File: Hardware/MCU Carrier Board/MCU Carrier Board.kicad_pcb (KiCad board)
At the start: 2 copper layers, 31.8 x 50.8 mm, 27 parts, among them J1 Conn_01x06_Pin, J2 Conn_01x06_Pin, J3 Conn_01x06_Pin, J4 Top Connector, J5 Bottom Connector, J6 Conn_01x06_Pin, J7 Conn_01x06_Pin, J8 Conn_01x06_Pin, SW3 SW_Push, SW4 SW_Push, SW5 SW_Push

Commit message: update
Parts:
- C1, C2, C3, C4: footprint Capacitor_SMD:C_0603_1608Metric_Pad1.08x0.95mm_HandSolder -> MCU Carrier board:C_0603_1608Metric_Pad1.08x0.95mm_HandSolder
- D1, D2, D3, D4: footprint LED_SMD:LED_0603_1608Metric_Pad1.05x0.95mm_HandSolder -> MCU Carrier board:LED_0603_1608Metric_Pad1.05x0.95mm_HandSolder
- H1, H2, H3, H4: footprint MountingHole:MountingHole_2.5mm -> MCU Carrier board:MountingHole_2.5mm
- J1, J2, J3, J6, J7, J8: footprint Connector_PinHeader_1.27mm:PinHeader_1x06_P1.27mm_Vertical -> MCU Carrier board:PinHeader_1x06_P1.27mm_Vertical
- J4, J5: footprint DF40C:HRS_DF40C-20DS-0.4V_51_ -> MCU Carrier board:HRS_DF40C-20DS-0.4V_51_
- R1, R2, R3, R4: footprint Resistor_SMD:R_0603_1608Metric_Pad0.98x0.95mm_HandSolder -> MCU Carrier board:R_0603_1608Metric_Pad0.98x0.95mm_HandSolder
- SW3, SW4, SW5: footprint Button_Switch_SMD:SW_Push_1P1T_XKB_TS-1187A -> MCU Carrier board:SW_Push_1P1T_XKB_TS-1187A
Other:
- board text added: "MCU R V1 10/25"
- board text added: "Up"

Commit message: update
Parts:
- C1, C2, C3, C4: footprint MCU Carrier board:C_0603_1608Metric_Pad1.08x0.95mm_HandSolder -> MCU_Controller:C_0603_1608Metric_Pad1.08x0.95mm_HandSolder
- D1, D2, D3, D4: footprint MCU Carrier board:LED_0603_1608Metric_Pad1.05x0.95mm_HandSolder -> MCU_Controller:LED_0603_1608Metric_Pad1.05x0.95mm_HandSolder
- H1, H2, H3, H4: footprint MCU Carrier board:MountingHole_2.5mm -> MCU_Controller:MountingHole_2.5mm
- J1, J2, J3, J6, J7, J8: footprint MCU Carrier board:PinHeader_1x06_P1.27mm_Vertical -> MCU_Controller:PinHeader_1x06_P1.27mm_Vertical
- J4, J5: footprint MCU Carrier board:HRS_DF40C-20DS-0.4V_51_ -> MCU_Controller:HRS_DF40C-20DS-0.4V_51_
- R1, R2, R3, R4: footprint MCU Carrier board:R_0603_1608Metric_Pad0.98x0.95mm_HandSolder -> MCU_Controller:R_0603_1608Metric_Pad0.98x0.95mm_HandSolder
- SW3, SW4, SW5: footprint MCU Carrier board:SW_Push_1P1T_XKB_TS-1187A -> MCU_Controller:SW_Push_1P1T_XKB_TS-1187A
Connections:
- J2 pad 5: unconnected-(J2-Pin_5-Pad5) -> GPIO39
- J5 pad 15: GND -> GPIO39
- J5 pad 17: GND -> GPIO40
- J7 pad 2: unconnected-(J7-Pin_2-Pad2) -> GPIO40
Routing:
- net GPIO39: track 0.00 -> 27.3 mm, vias 0 -> 1
- net GPIO40: track 0.00 -> 15.5 mm, vias 0 -> 1
- net VCC_5V: track 9.49 -> 10.6 mm

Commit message: added test points
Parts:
- added 3V3: TestPoint, TestPoint:TestPoint_Pad_D1.0mm, F.Cu at (157.8, 92.9)
- added Gnd1: TestPoint, TestPoint:TestPoint_Pad_D1.0mm, F.Cu at (157.8, 87.9)
- added VBUS1: TestPoint, TestPoint:TestPoint_Pad_D1.0mm, F.Cu at (140.0, 63.1)
- C1, C2, C3, C4: footprint MCU_Controller:C_0603_1608Metric_Pad1.08x0.95mm_HandSolder -> Capacitor_SMD:C_0603_1608Metric_Pad1.08x0.95mm_HandSolder
- D1, D2, D3, D4: footprint MCU_Controller:LED_0603_1608Metric_Pad1.05x0.95mm_HandSolder -> LED_SMD:LED_0603_1608Metric_Pad1.05x0.95mm_HandSolder
- H1, H2, H3, H4: footprint MCU_Controller:MountingHole_2.5mm -> MountingHole:MountingHole_2.5mm
- J1, J2, J3, J6, J7, J8: footprint MCU_Controller:PinHeader_1x06_P1.27mm_Vertical -> Connector_PinHeader_1.27mm:PinHeader_1x06_P1.27mm_Vertical
- J4, J5: footprint MCU_Controller:HRS_DF40C-20DS-0.4V_51_ -> DF40C:HRS_DF40C-20DS-0.4V_51_
- R1, R2, R3, R4: footprint MCU_Controller:R_0603_1608Metric_Pad0.98x0.95mm_HandSolder -> Resistor_SMD:R_0603_1608Metric_Pad0.98x0.95mm_HandSolder
- SW3, SW4, SW5: footprint MCU_Controller:SW_Push_1P1T_XKB_TS-1187A -> Button_Switch_SMD:SW_Push_1P1T_XKB_TS-1187A
- moved SW3 0.75 mm to (145.9, 61.8)
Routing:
- net VCC_3V3: track 130.9 -> 135.0 mm
- net GND: track 6.90 -> 10.4 mm
- net VCC_5V: track 10.6 -> 13.3 mm
- net GPIO21: track 13.1 -> 12.4 mm

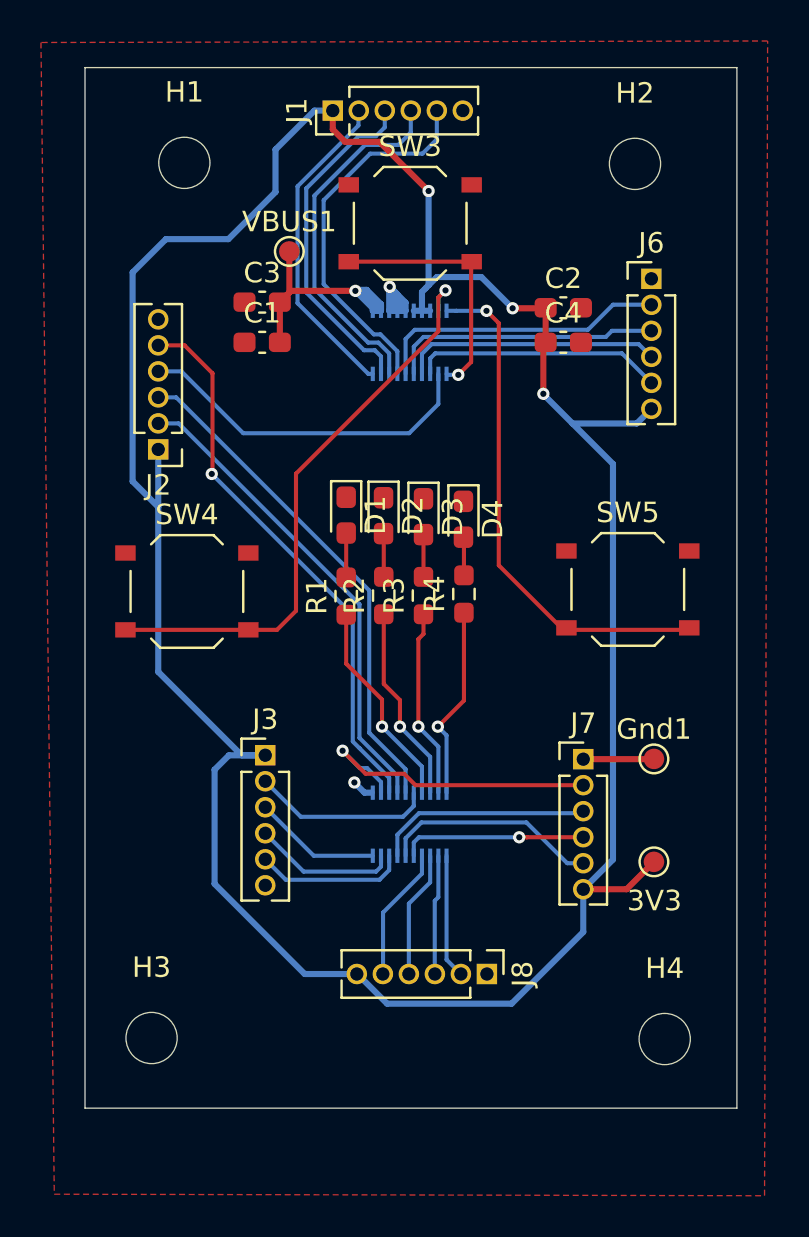
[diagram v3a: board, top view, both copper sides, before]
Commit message: updated footprints
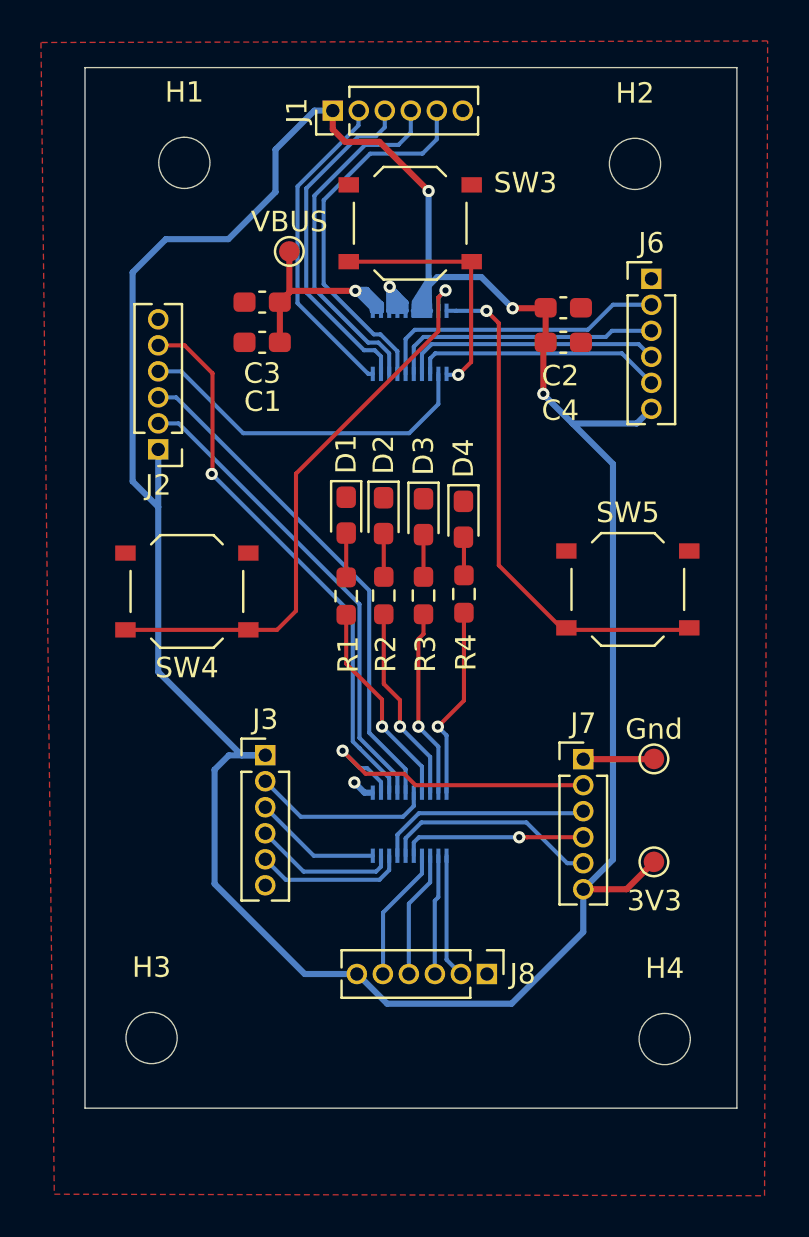
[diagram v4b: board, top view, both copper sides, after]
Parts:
- 3V3: footprint TestPoint:TestPoint_Pad_D1.0mm -> MCU_Carrier_Board:TestPoint_Pad_D1.0mm
- C1, C2, C3, C4: footprint Capacitor_SMD:C_0603_1608Metric_Pad1.08x0.95mm_HandSolder -> MCU_Carrier_Board:C_0603_1608Metric_Pad1.08x0.95mm_HandSolder
- D1, D2, D3, D4: footprint LED_SMD:LED_0603_1608Metric_Pad1.05x0.95mm_HandSolder -> MCU_Carrier_Board:LED_0603_1608Metric_Pad1.05x0.95mm_HandSolder
- Gnd: renamed from Gnd1; footprint TestPoint:TestPoint_Pad_D1.0mm -> MCU_Carrier_Board:TestPoint_Pad_D1.0mm
- H1, H2, H3, H4: footprint MountingHole:MountingHole_2.5mm -> MCU_Carrier_Board:MountingHole_2.5mm
- J1, J2, J3, J6, J7, J8: footprint Connector_PinHeader_1.27mm:PinHeader_1x06_P1.27mm_Vertical -> MCU_Carrier_Board:PinHeader_1x06_P1.27mm_Vertical
- J4, J5: footprint DF40C:HRS_DF40C-20DS-0.4V_51_ -> MCU_Carrier_Board:HRS_DF40C-20DS-0.4V_51_
- R1, R2, R3, R4: footprint Resistor_SMD:R_0603_1608Metric_Pad0.98x0.95mm_HandSolder -> MCU_Carrier_Board:R_0603_1608Metric_Pad0.98x0.95mm_HandSolder
- SW3, SW4, SW5: footprint Button_Switch_SMD:SW_Push_1P1T_XKB_TS-1187A -> MCU_Carrier_Board:SW_Push_1P1T_XKB_TS-1187A
- VBUS: renamed from VBUS1; footprint TestPoint:TestPoint_Pad_D1.0mm -> MCU_Carrier_Board:TestPoint_Pad_D1.0mm
